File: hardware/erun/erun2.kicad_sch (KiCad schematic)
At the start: 34 parts, among them J1 Conn_Coaxial, J10 Conn_01x03_Female, J2 HEIDENHAIN_MT25_TTL, J3 TRIGGER_TTL, J4 Conn_01x02_Female, J5 Conn_01x02_Female, J6 Conn_01x02_Female, J7 Conn_01x02_Female, J8 Conn_01x02_Female, J9 Conn_01x03_Female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

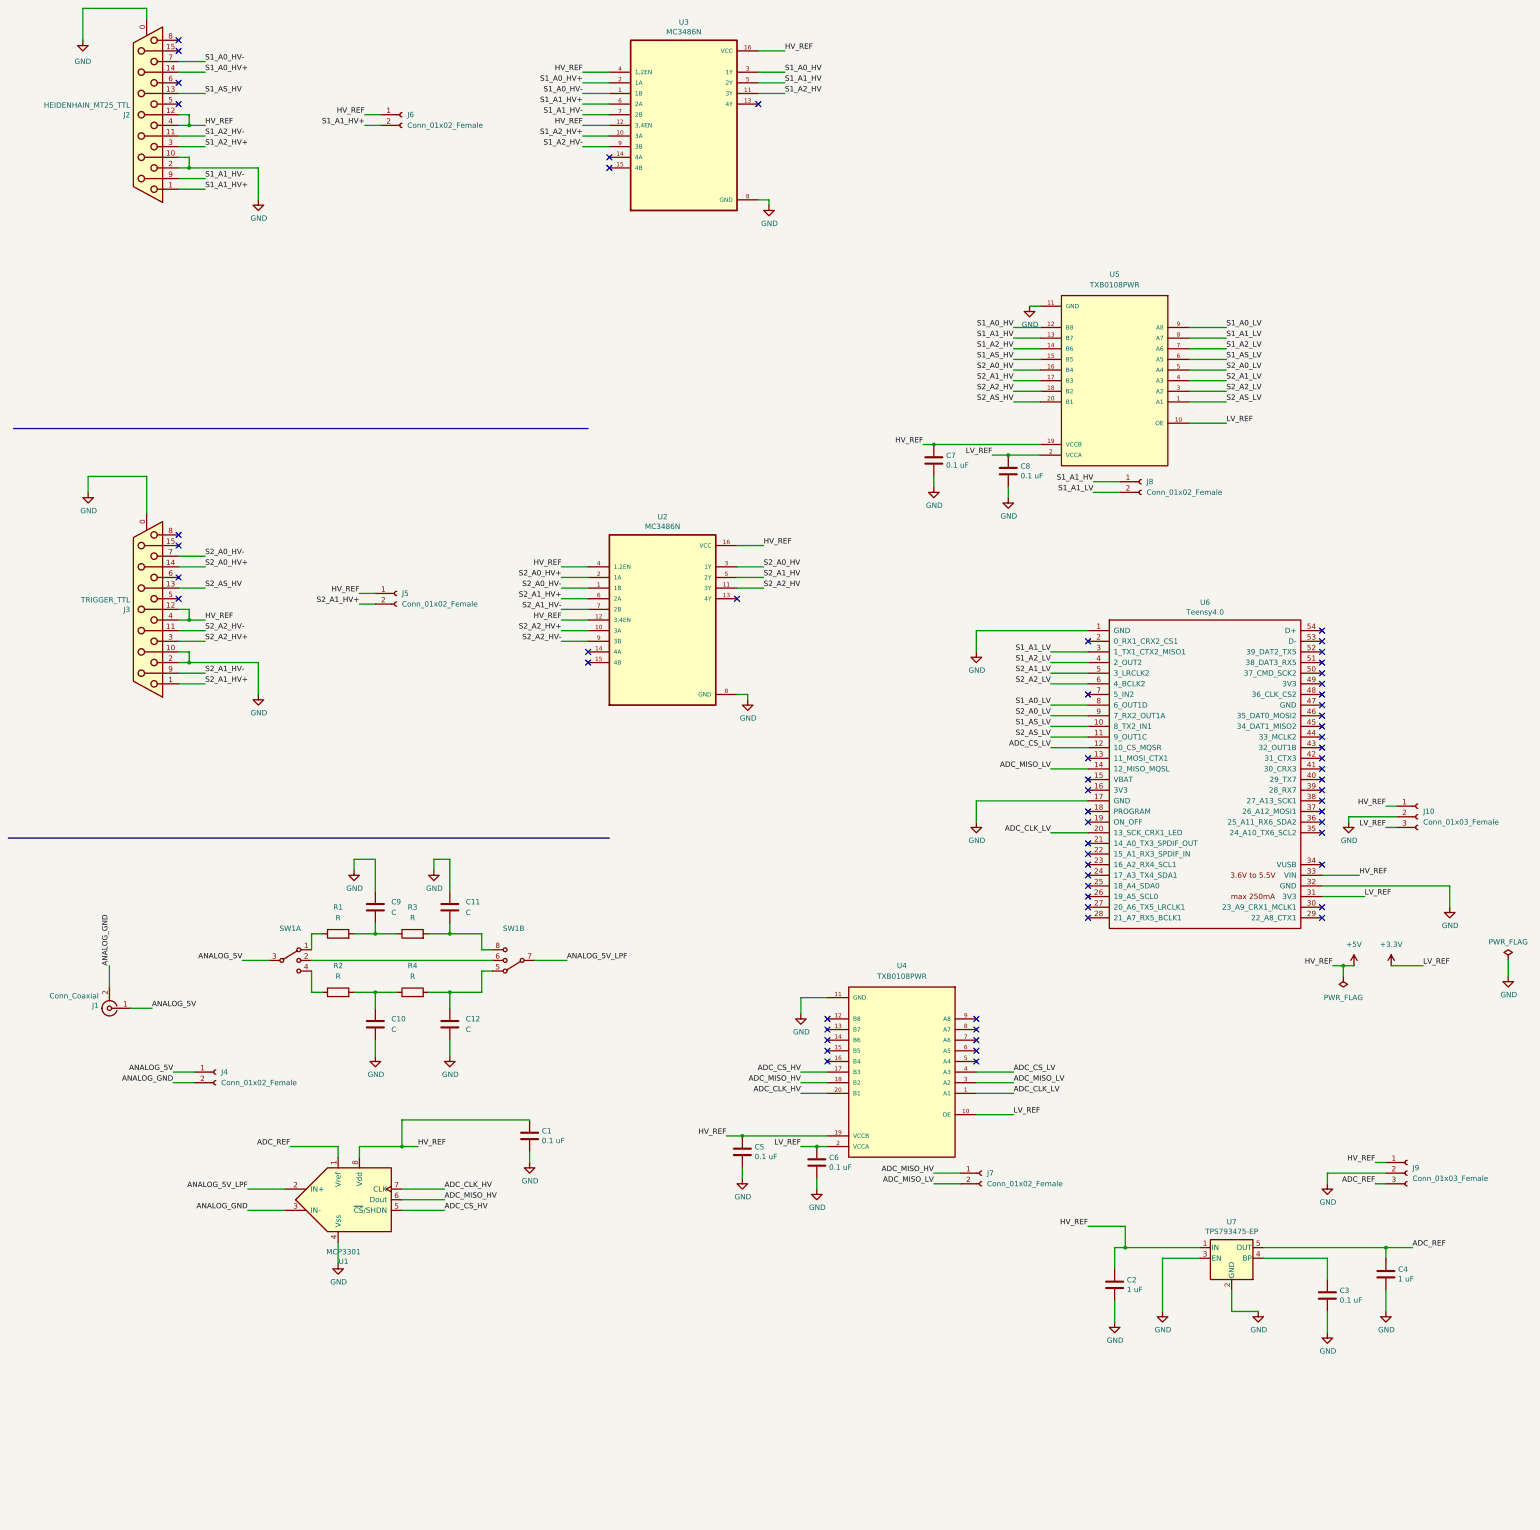
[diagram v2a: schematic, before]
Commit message: Updated some labels
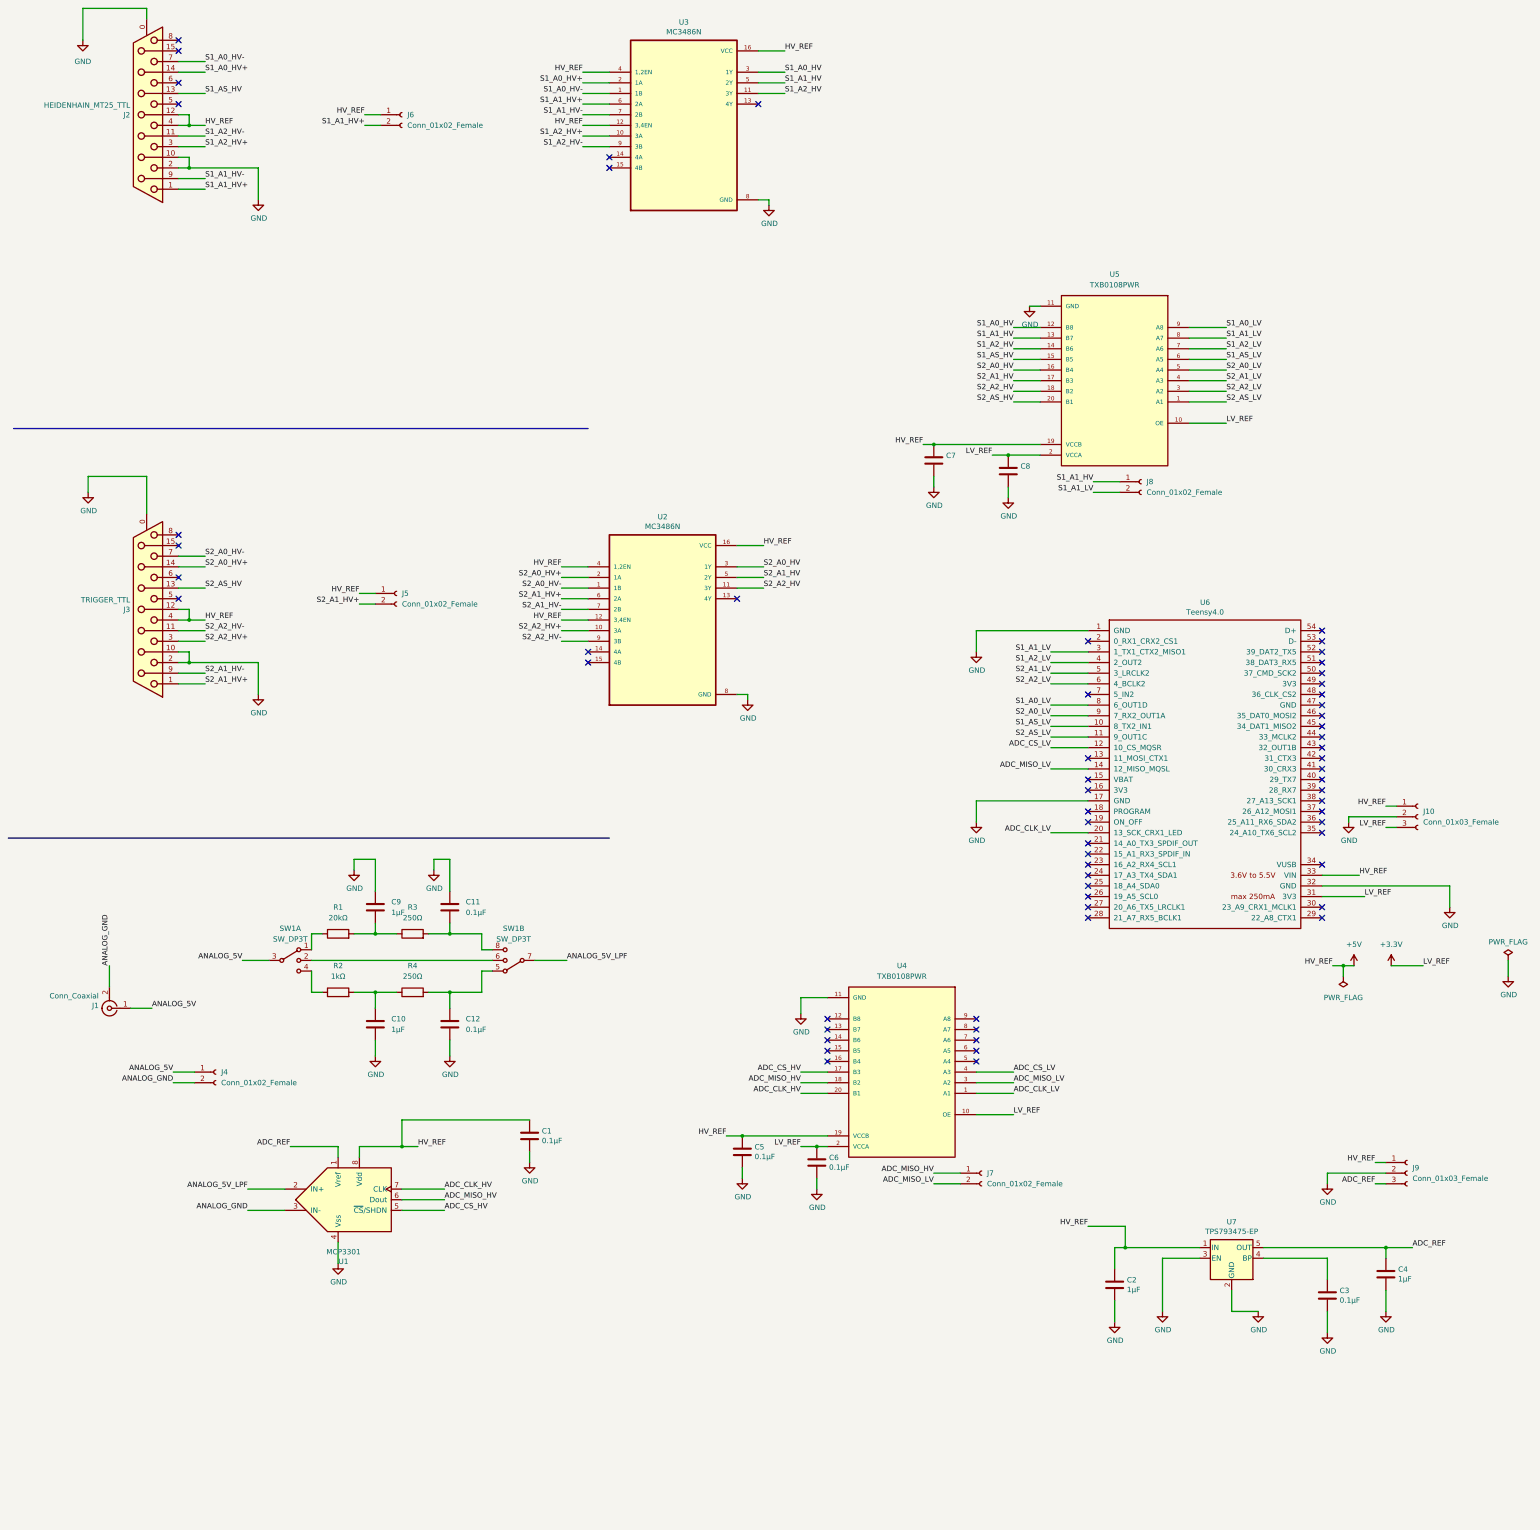
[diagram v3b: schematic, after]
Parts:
- C1, C3, C5, C6: value 0.1 uF -> 0.1μF
- C10, C9: value C -> 1μF
- C11, C12: value C -> 0.1μF
- C2, C4: value 1 uF -> 1μF
- C7, C8: value 0.1 uF -> (none)
- R1: value R -> 20kΩ
- R2: value R -> 1kΩ
- R3, R4: value R -> 250Ω
- SW1: value (none) -> SW_DP3T; footprint (none) -> SW_DP3T:SW_DP3T
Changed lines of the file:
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@@
       (effects (font (size 1.27 1.27)) (justify left))
     )
-    (property "Value" "0.1 uF" (id 1) (at 330.581 342.773 0)
+    (property "Value" "0.1μF" (id 1) (at 330.581 342.773 0)
       (effects (font (size 1.27 1.27)) (justify left))
     )
@@
       (effects (font (size 1.27 1.27)) (justify left))
     )
-    (property "Value" "1 uF" (id 1) (at 344.551 337.693 0)
+    (property "Value" "1μF" (id 1) (at 344.551 337.693 0)
       (effects (font (size 1.27 1.27)) (justify left))
     )
@@
       (effects (font (size 1.27 1.27)) (justify left))
     )
-    (property "Value" "1 uF" (id 1) (at 279.781 340.233 0)
+    (property "Value" "1μF" (id 1) (at 279.781 340.233 0)
       (effects (font (size 1.27 1.27)) (justify left))
     )
@@
       (effects (font (size 1.27 1.27)) (justify left))
     )
-    (property "Value" "0.1 uF" (id 1) (at 140.081 304.673 0)
+    (property "Value" "0.1μF" (id 1) (at 140.081 304.673 0)
       (effects (font (size 1.27 1.27)) (justify left))
     )
@@
       (effects (font (size 1.27 1.27)) (justify left))
     )
-    (property "Value" "0.1 uF" (id 1) (at 236.601 143.383 0)
+    (property "Value" "" (id 1) (at 236.601 143.383 0)
       (effects (font (size 1.27 1.27)) (justify left))
     )
@@
     (in_bom yes) (on_board yes) (fields_autoplaced)
     (property "Reference" "R3" (id 0) (at 109.22 248.92 90))
-    (property "Value" "R" (id 1) (at 109.22 251.46 90))
+    (property "Value" "250Ω" (id 1) (at 109.22 251.46 90))
     (property "Footprint" "Resistor_SMD:R_0603_1608Metric" (id 2) (at 109.22 257.048 90)
       (effects (font (size 1.27 1.27)) hide)
@@
       (effects (font (size 1.27 1.27)) (justify left))
     )
-    (property "Value" "0.1 uF" (id 1) (at 190.881 308.483 0)
+    (property "Value" "0.1μF" (id 1) (at 190.881 308.483 0)
       (effects (font (size 1.27 1.27)) (justify left))
     )
@@
       (effects (font (size 1.27 1.27)) (justify left))
     )
-    (property "Value" "C" (id 1) (at 121.92 250.1899 0)
+    (property "Value" "0.1μF" (id 1) (at 121.92 250.1899 0)
       (effects (font (size 1.27 1.27)) (justify left))
     )
@@
     (in_bom yes) (on_board yes) (fields_autoplaced)
     (property "Reference" "R1" (id 0) (at 91.44 248.92 90))
-    (property "Value" "R" (id 1) (at 91.44 251.46 90))
+    (property "Value" "20kΩ" (id 1) (at 91.44 251.46 90))
     (property "Footprint" "Resistor_SMD:R_0603_1608Metric" (id 2) (at 91.44 257.048 90)
       (effects (font (size 1.27 1.27)) hide)
@@
     (in_bom yes) (on_board yes) (fields_autoplaced)
     (property "Reference" "SW1" (id 0) (at 133.35 254 0))
-    (property "Value" "" (id 1) (at 133.35 256.54 0))
-    (property "Footprint" "" (id 2) (at 149.225 266.065 0)
+    (property "Value" "SW_DP3T" (id 1) (at 133.35 256.54 0))
+    (property "Footprint" "SW_DP3T:SW_DP3T" (id 2) (at 149.225 266.065 0)
       (effects (font (size 1.27 1.27)) hide)
     )
@@
       (effects (font (size 1.27 1.27)) (justify left))
     )
-    (property "Value" "C" (id 1) (at 121.92 278.1299 0)
+    (property "Value" "0.1μF" (id 1) (at 121.92 278.1299 0)
       (effects (font (size 1.27 1.27)) (justify left))
     )
@@
     (in_bom yes) (on_board yes) (fields_autoplaced)
     (property "Reference" "SW1" (id 0) (at 80.01 254 0))
-    (property "Value" "" (id 1) (at 80.01 256.54 0))
-    (property "Footprint" "" (id 2) (at 64.135 257.175 0)
+    (property "Value" "SW_DP3T" (id 1) (at 80.01 256.54 0))
+    (property "Footprint" "SW_DP3T:SW_DP3T" (id 2) (at 64.135 257.175 0)
       (effects (font (size 1.27 1.27)) hide)
     )
@@
     (in_bom yes) (on_board yes) (fields_autoplaced)
     (property "Reference" "R4" (id 0) (at 109.22 262.89 90))
-    (property "Value" "R" (id 1) (at 109.22 265.43 90))
+    (property "Value" "250Ω" (id 1) (at 109.22 265.43 90))
     (property "Footprint" "Resistor_SMD:R_0603_1608Metric" (id 2) (at 109.22 271.018 90)
       (effects (font (size 1.27 1.27)) hide)
@@
       (effects (font (size 1.27 1.27)) (justify left))
     )
-    (property "Value" "0.1 uF" (id 1) (at 254.381 145.923 0)
+    (property "Value" "" (id 1) (at 254.381 145.923 0)
       (effects (font (size 1.27 1.27)) (justify left))
     )
@@
       (effects (font (size 1.27 1.27)) (justify left))
     )
-    (property "Value" "C" (id 1) (at 104.14 250.1899 0)
+    (property "Value" "1μF" (id 1) (at 104.14 250.1899 0)
       (effects (font (size 1.27 1.27)) (justify left))
     )
@@
       (effects (font (size 1.27 1.27)) (justify left))
     )
-    (property "Value" "C" (id 1) (at 104.14 278.1299 0)
+    (property "Value" "1μF" (id 1) (at 104.14 278.1299 0)
       (effects (font (size 1.27 1.27)) (justify left))
     )
@@
     (in_bom yes) (on_board yes) (fields_autoplaced)
     (property "Reference" "R2" (id 0) (at 91.44 262.89 90))
-    (property "Value" "R" (id 1) (at 91.44 265.43 90))
+    (property "Value" "1kΩ" (id 1) (at 91.44 265.43 90))
     (property "Footprint" "Resistor_SMD:R_0603_1608Metric" (id 2) (at 91.44 271.018 90)
       (effects (font (size 1.27 1.27)) hide)
@@
       (effects (font (size 1.27 1.27)) (justify left))
     )
-    (property "Value" "0.1 uF" (id 1) (at 208.661 311.023 0)
+    (property "Value" "0.1μF" (id 1) (at 208.661 311.023 0)
       (effects (font (size 1.27 1.27)) (justify left))
     )
@@
     )
     (path "/00000000-0000-0000-0000-000061e50296"
-      (reference "C1") (unit 1) (value "0.1 uF") (footprint "Capacitor_SMD:C_0603_1608Metric")
+      (reference "C1") (unit 1) (value "0.1μF") (footprint "Capacitor_SMD:C_0603_1608Metric")
     )
     (path "/00000000-0000-0000-0000-000061dc0488"
-      (reference "C2") (unit 1) (value "1 uF") (footprint "Capacitor_SMD:C_0603_1608Metric")
+      (reference "C2") (unit 1) (value "1μF") (footprint "Capacitor_SMD:C_0603_1608Metric")
     )
     (path "/00000000-0000-0000-0000-000061d89473"
-      (reference "C3") (unit 1) (value "0.1 uF") (footprint "Capacitor_SMD:C_0603_1608Metric")
+      (reference "C3") (unit 1) (value "0.1μF") (footprint "Capacitor_SMD:C_0603_1608Metric")
     )
     (path "/00000000-0000-0000-0000-000061dad5ec"
-      (reference "C4") (unit 1) (value "1 uF") (footprint "Capacitor_SMD:C_0603_1608Metric")
+      (reference "C4") (unit 1) (value "1μF") (footprint "Capacitor_SMD:C_0603_1608Metric")
     )
     (path "/48efb94c-7490-48b7-985d-5d498ebcf74d"
-      (reference "C5") (unit 1) (value "0.1 uF") (footprint "Capacitor_SMD:C_0603_1608Metric")
+      (reference "C5") (unit 1) (value "0.1μF") (footprint "Capacitor_SMD:C_0603_1608Metric")
     )
     (path "/f85937f8-33ae-41b5-b986-41f51af36c4e"
-      (reference "C6") (unit 1) (value "0.1 uF") (footprint "Capacitor_SMD:C_0603_1608Metric")
+      (reference "C6") (unit 1) (value "0.1μF") (footprint "Capacitor_SMD:C_0603_1608Metric")
     )
     (path "/2f4d3bb5-3168-46f9-b83e-9f683cf45b44"
-      (reference "C7") (unit 1) (value "0.1 uF") (footprint "Capacitor_SMD:C_0603_1608Metric")
+      (reference "C7") (unit 1) (value "0.1μF") (footprint "Capacitor_SMD:C_0603_1608Metric")
     )
     (path "/c695cb4e-a3d8-4ba7-be3f-1295c970652c"
-      (reference "C8") (unit 1) (value "0.1 uF") (footprint "Capacitor_SMD:C_0603_1608Metric")
+      (reference "C8") (unit 1) (value "0.1μF") (footprint "Capacitor_SMD:C_0603_1608Metric")
     )
     (path "/cc7b1613-1929-42d4-b418-4bd868b9f0a3"
-      (reference "C9") (unit 1) (value "C") (footprint "Capacitor_SMD:C_0603_1608Metric")
+      (reference "C9") (unit 1) (value "1μF") (footprint "Capacitor_SMD:C_0603_1608Metric")
     )
     (path "/ce70db6f-09be-49fe-9f52-2be231e70357"
-      (reference "C10") (unit 1) (value "C") (footprint "Capacitor_SMD:C_0603_1608Metric")
+      (reference "C10") (unit 1) (value "1μF") (footprint "Capacitor_SMD:C_0603_1608Metric")
     )
     (path "/502c4f14-d253-48e3-8eef-84834a6d8adb"
-      (reference "C11") (unit 1) (value "C") (footprint "Capacitor_SMD:C_0603_1608Metric")
+      (reference "C11") (unit 1) (value "0.1μF") (footprint "Capacitor_SMD:C_0603_1608Metric")
     )
     (path "/9b51d0a2-c117-471e-a5e0-7d6e515c7ce6"
-      (reference "C12") (unit 1) (value "C") (footprint "Capacitor_SMD:C_0603_1608Metric")
+      (reference "C12") (unit 1) (value "0.1μF") (footprint "Capacitor_SMD:C_0603_1608Metric")
     )
     (path "/00000000-0000-0000-0000-0000619e4137"
@@
     )
     (path "/70a09bf0-5e27-4706-81bb-98a5cf06fcc9"
-      (reference "R1") (unit 1) (value "R") (footprint "Resistor_SMD:R_0603_1608Metric")
+      (reference "R1") (unit 1) (value "20kΩ") (footprint "Resistor_SMD:R_0603_1608Metric")
     )
     (path "/ea1d30ec-785e-440f-9954-8ce920692da1"
-      (reference "R2") (unit 1) (value "R") (footprint "Resistor_SMD:R_0603_1608Metric")
+      (reference "R2") (unit 1) (value "1kΩ") (footprint "Resistor_SMD:R_0603_1608Metric")
     )
     (path "/3cc7e990-93d6-41f7-94d4-0eba250e47f7"
-      (reference "R3") (unit 1) (value "R") (footprint "Resistor_SMD:R_0603_1608Metric")
+      (reference "R3") (unit 1) (value "250Ω") (footprint "Resistor_SMD:R_0603_1608Metric")
     )
     (path "/bdfd0ae7-37e1-4d4b-9ac4-c6985a47e38c"
-      (reference "R4") (unit 1) (value "R") (footprint "Resistor_SMD:R_0603_1608Metric")
+      (reference "R4") (unit 1) (value "250Ω") (footprint "Resistor_SMD:R_0603_1608Metric")
     )
     (path "/bd572dac-350f-4d4c-bd5b-e852715803a2"
